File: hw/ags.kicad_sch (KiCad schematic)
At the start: 23 parts, among them J1 Screw_Terminal_01x08, J2 SWD/ARM10, J3 Conn_02x03_Odd_Even, J4 Conn_01x05, SW1 PTS526SM15SMTR2 LFS, U12 NV24C08DWVLT3G, U5 ESP32-S3-MINI-1

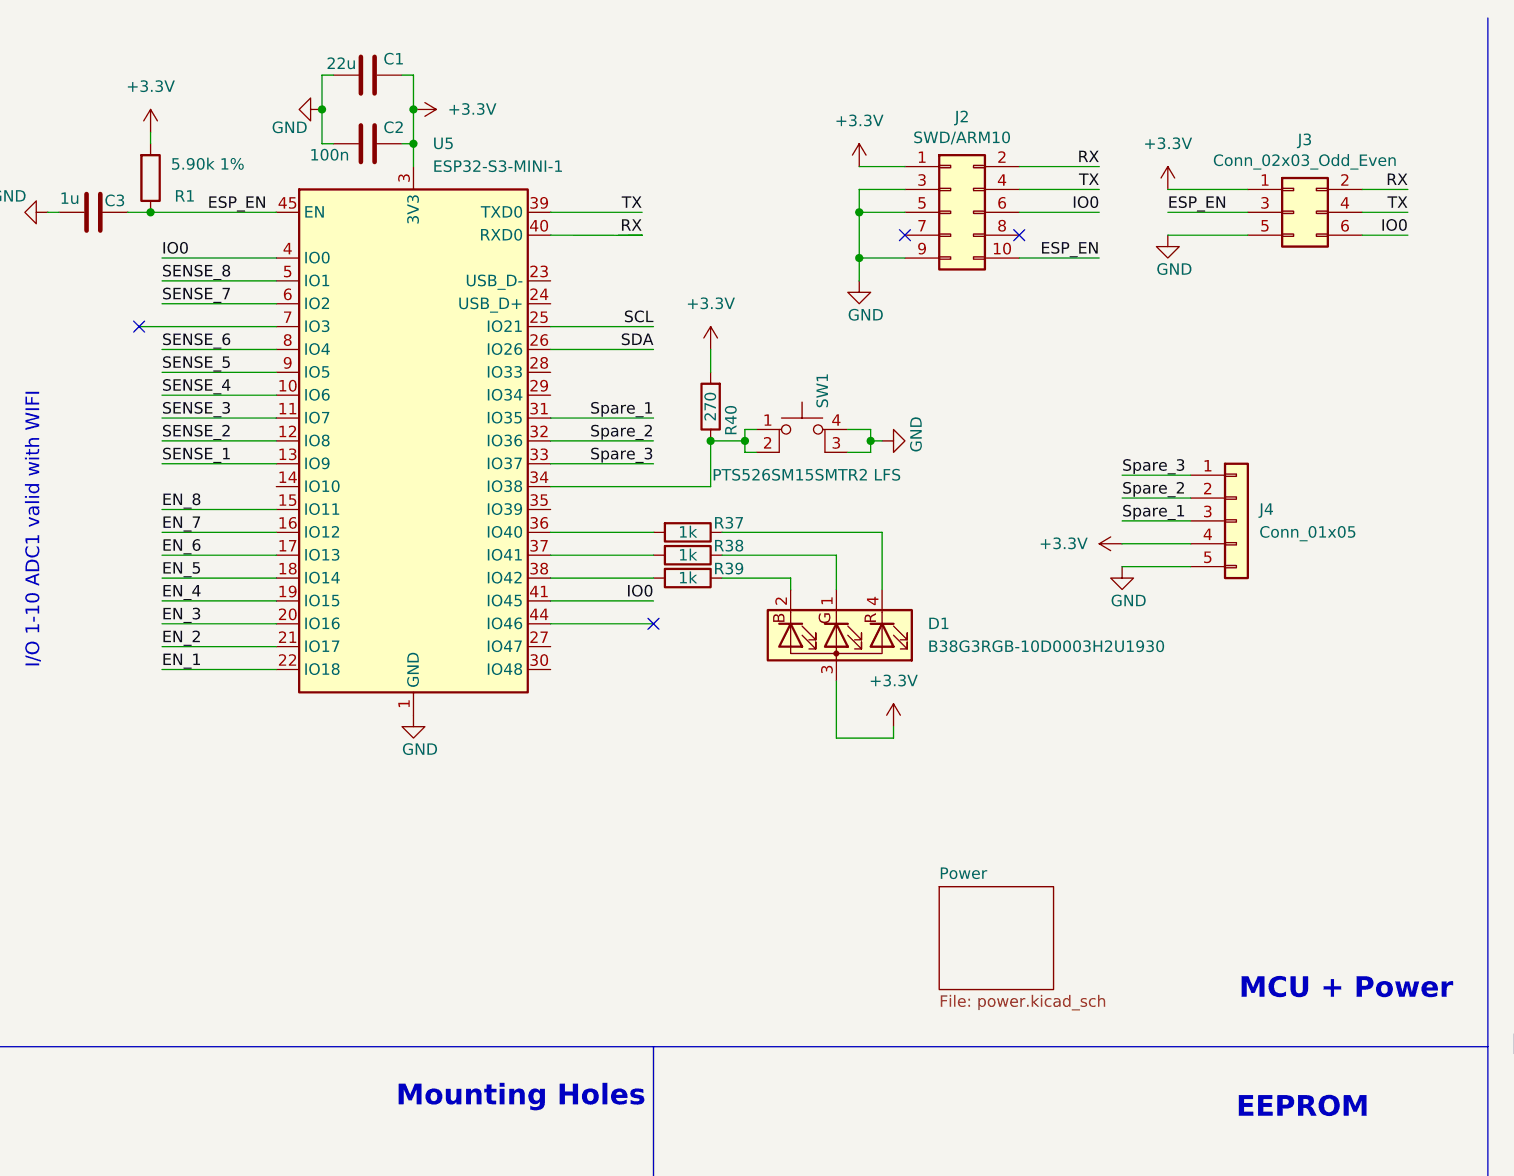
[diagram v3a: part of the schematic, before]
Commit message: Added sense for input voltage and created BOM
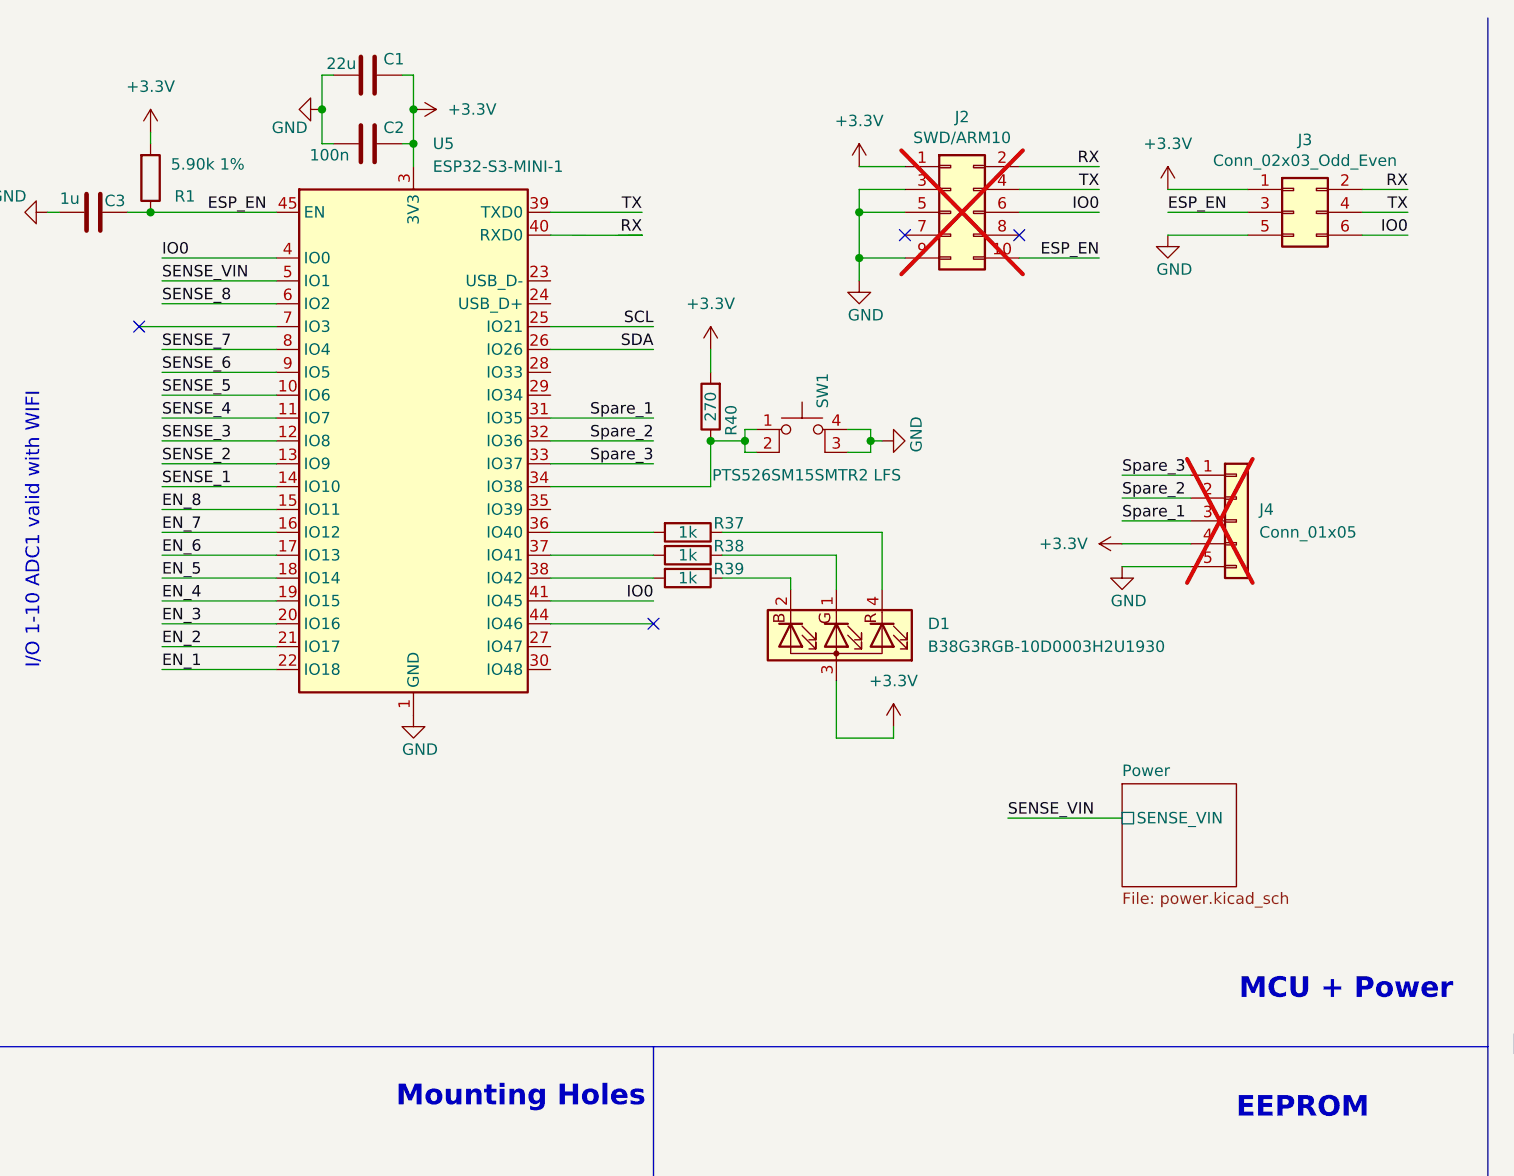
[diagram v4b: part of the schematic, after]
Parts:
- C1: Manufacturer Part Number (none) -> JMK212BBJ226MGHT
- C2: Manufacturer Part Number (none) -> CL10B104KC8NNNC
- C3, C4: Manufacturer Part Number (none) -> CL10B105KP8NNNC
- D1: Manufacturer Part Number (none) -> B38G3RGB-10D0003H2U1930
- J1: Manufacturer Part Number (none) -> QT08ASF83H0000G
- J2, J4: now not fitted
- R1, R15, R19: Manufacturer Part Number (none) -> AC0603FR-075K9L
- R37, R38, R39: Manufacturer Part Number (none) -> RMCF0603JT1K00
- R40: Manufacturer Part Number (none) -> RMCF0603JT270R
- SW1: Manufacturer Part Number (none) -> PTS526SM15SMTR2 LFS
- U12: Manufacturer Part Number (none) -> NV24C08DWVLT3G
- U5: Manufacturer Part Number (none) -> ESP32-S3-MINI-1-N8
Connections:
- net SENSE_1: now also U5.14 (IO10); no longer U5.13 (IO9)
- net SENSE_2: now also U5.13 (IO9); no longer U5.12 (IO8)
- net SENSE_3: now also U5.12 (IO8); no longer U5.11 (IO7)
- net SENSE_4: now also U5.11 (IO7); no longer U5.10 (IO6)
- net SENSE_5: now also U5.10 (IO6); no longer U5.9 (IO5)
- net SENSE_6: now also U5.9 (IO5); no longer U5.8 (IO4)
- net SENSE_7: now also U5.8 (IO4); no longer U5.6 (IO2)
- net SENSE_8: now also U5.6 (IO2); no longer U5.5 (IO1)
- new net SENSE_VIN: U5.5 (IO1)
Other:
- sheet Power ports: added SENSE_VIN; removed none
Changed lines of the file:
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@@
 	(wire
 		(pts
+			(xy 33.02 64.77) (xy 45.72 64.77)
+		)
+		(stroke
+			(width 0)
+			(type default)
+		)
+	)
+	(wire
+		(pts
 			(xy 115.57 29.21) (xy 110.49 29.21)
 		)
@@
 	(wire
 		(pts
+			(xy 127 101.6) (xy 139.7 101.6)
+		)
+		(stroke
+			(width 0)
+			(type default)
+		)
+	)
+	(wire
+		(pts
 			(xy 236.22 41.91) (xy 248.92 41.91)
 		)
@@
 	)
 	(label "SENSE_2"
-		(at 33.02 59.69 0)
+		(at 33.02 62.23 0)
 		(effects
 			(font
@@
 	)
 	(label "SENSE_1"
-		(at 33.02 62.23 0)
+		(at 33.02 64.77 0)
 		(effects
 			(font
@@
 	)
 	(label "SENSE_4"
-		(at 33.02 54.61 0)
+		(at 33.02 57.15 0)
 		(effects
 			(font
@@
 		)
 	)
+	(label "SENSE_VIN"
+		(at 127 101.6 0)
+		(effects
+			(font
+				(size 1.27 1.27)
+			)
+			(justify left bottom)
+		)
+	)
 	(label "COMM_V"
 		(at 238.76 74.93 0)
@@
 	)
 	(label "SENSE_8"
-		(at 33.02 41.91 0)
+		(at 33.02 44.45 0)
 		(effects
 			(font
@@
 		)
 	)
+	(label "SENSE_VIN"
+		(at 33.02 41.91 0)
+		(effects
+			(font
+				(size 1.27 1.27)
+			)
+			(justify left bottom)
+		)
+	)
 	(label "TX"
 		(at 171.45 34.29 180)
@@
 	)
 	(label "SENSE_6"
-		(at 33.02 49.53 0)
+		(at 33.02 52.07 0)
 		(effects
 			(font
@@
 	)
 	(label "SENSE_3"
-		(at 33.02 57.15 0)
+		(at 33.02 59.69 0)
 		(effects
 			(font
@@
 	)
 	(label "SENSE_7"
-		(at 33.02 44.45 0)
+		(at 33.02 49.53 0)
 		(effects
 			(font
@@
 	)
 	(label "SENSE_5"
-		(at 33.02 52.07 0)
+		(at 33.02 54.61 0)
 		(effects
 			(font
@@
 		(in_bom yes)
 		(on_board yes)
-		(dnp no)
+		(dnp yes)
 		(property "Reference" "J2"
 			(at 121.92 23.6982 0)
@@
 			)
 		)
+		(property "Manufacturer Part Number" "RMCF0603JT1K00"
+			(at 91.44 72.39 90)
+			(effects
+				(font
+					(size 1.27 1.27)
+				)
+				(hide yes)
+			)
+		)
 		(pin "1"
 		)
@@
 			)
 		)
+		(property "Manufacturer Part Number" "CL10B104KC8NNNC"
+			(at 55.88 26.67 90)
+			(effects
+				(font
+					(size 1.27 1.27)
+				)
+				(hide yes)
+			)
+		)
 		(pin "1"
 		)
@@
 			)
 		)
+		(property "Manufacturer Part Number" "B38G3RGB-10D0003H2U1930"
+			(at 107.95 81.28 90)
+			(effects
+				(font
+					(size 1.27 1.27)
+				)
+				(hide yes)
+			)
+		)
 		(pin "3"
 		)
@@
 			)
 		)
+		(property "Manufacturer Part Number" "AC0603FR-075K9L"
+			(at 162.56 158.75 0)
+			(effects
+				(font
+					(size 1.27 1.27)
+				)
+				(hide yes)
+			)
+		)
 		(pin "1"
 		)
@@
 			)
 		)
+		(property "Manufacturer Part Number" "AC0603FR-075K9L"
+			(at 31.75 30.48 0)
+			(effects
+				(font
+					(size 1.27 1.27)
+				)
+				(hide yes)
+			)
+		)
 		(pin "1"
 		)
@@
 			)
 		)
+		(property "Manufacturer Part Number" "RMCF0603JT1K00"
+			(at 91.44 69.85 90)
+			(effects
+				(font
+					(size 1.27 1.27)
+				)
+				(hide yes)
+			)
+		)
 		(pin "1"
 		)
@@
 			)
 		)
+		(property "Manufacturer Part Number" "JMK212BBJ226MGHT"
+			(at 55.88 19.05 90)
+			(effects
+				(font
+					(size 1.27 1.27)
+				)
+				(hide yes)
+			)
+		)
 		(pin "1"
 		)
@@
 			)
 		)
+		(property "Manufacturer Part Number" "CL10B105KP8NNNC"
+			(at 109.22 167.64 90)
+			(effects
+				(font
+					(size 1.27 1.27)
+				)
+				(hide yes)
+			)
+		)
 		(pin "1"
 		)
@@
 			)
 		)
+		(property "Manufacturer Part Number" "NV24C08DWVLT3G"
+			(at 123.19 168.91 0)
+			(effects
+				(font
+					(size 1.27 1.27)
+				)
+				(hide yes)
+			)
+		)
 		(pin "3"
 		)
@@
 			)
 		)
+		(property "Manufacturer Part Number" "AC0603FR-075K9L"
+			(at 148.59 158.75 0)
+			(effects
+				(font
+					(size 1.27 1.27)
+				)
+				(hide yes)
+			)
+		)
 		(pin "1"
 		)
@@
 			)
 		)
+		(property "Manufacturer Part Number" "RMCF0603JT270R"
+			(at 93.98 55.88 90)
+			(effects
+				(font
+					(size 1.27 1.27)
+				)
+				(hide yes)
+			)
+		)
 		(pin "1"
 		)
@@
 		(in_bom yes)
 		(on_board yes)
-		(dnp no)
+		(dnp yes)
 		(fields_autoplaced yes)
 		(property "Reference" "J4"
@@
 			)
 		)
+		(property "Manufacturer Part Number" "ESP32-S3-MINI-1-N8"
+			(at 60.96 59.69 0)
+			(effects
+				(font
+					(size 1.27 1.27)
+				)
+				(hide yes)
+			)
+		)
 		(pin "7"
 		)
@@
 			)
 		)
+		(property "Manufacturer Part Number" "CL10B105KP8NNNC"
+			(at 25.4 34.29 90)
+			(effects
+				(font
+					(size 1.27 1.27)
+				)
+				(hide yes)
+			)
+		)
 		(pin "1"
 		)
@@
 			)
 		)
+		(property "Manufacturer Part Number" "QT08ASF83H0000G"
+			(at 219.71 137.16 0)
+			(effects
+				(font
+					(size 1.27 1.27)
+				)
+				(hide yes)
+			)
+		)
 		(pin "6"
 		)
@@
 			)
 		)
+		(property "Manufacturer Part Number" "PTS526SM15SMTR2 LFS"
+			(at 104.14 60.96 90)
+			(effects
+				(font
+					(size 1.27 1.27)
+				)
+				(hide yes)
+			)
+		)
 		(pin "3"
 		)
@@
 			)
 		)
+		(property "Manufacturer Part Number" "RMCF0603JT1K00"
+			(at 91.44 74.93 90)
+			(effects
+				(font
+					(size 1.27 1.27)
+				)
+				(hide yes)
+			)
+		)
 		(pin "1"
 		)
@@
 	)
 	(sheet
-		(at 119.38 109.22)
+		(at 139.7 97.79)
 		(size 12.7 11.43)
 		(exclude_from_sim no)
@@
 		)
 		(property "Sheetname" "Power"
-			(at 119.38 108.5084 0)
+			(at 139.7 97.0784 0)
 			(effects
 				(font
@@
 		)
 		(property "Sheetfile" "power.kicad_sch"
-			(at 119.38 121.2346 0)
+			(at 139.7 109.8046 0)
 			(effects
 				(font
@@
 			)
 		)
+		(pin "SENSE_VIN" passive
+			(at 139.7 101.6 180)
+			(effects
+				(font
+					(size 1.27 1.27)
+				)
+				(justify left)
+			)
+		)

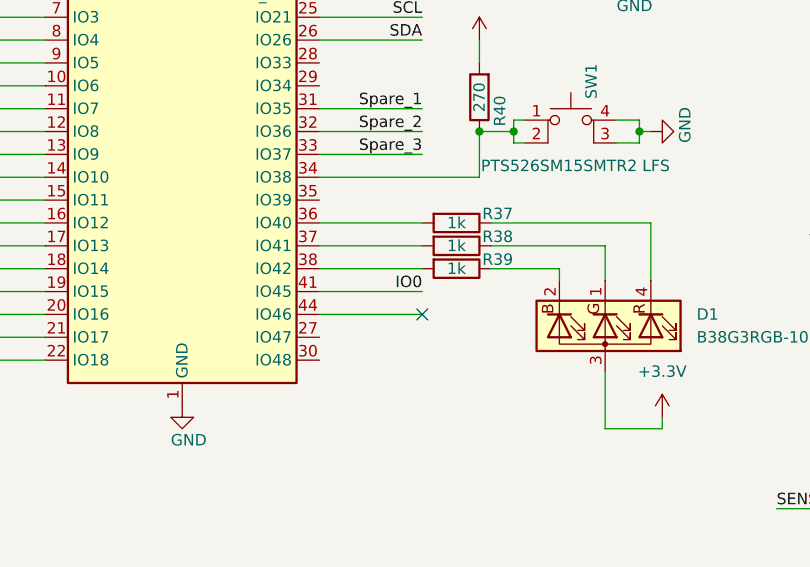
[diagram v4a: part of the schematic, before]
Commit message: Fixed button footprint and layout, fixed IO0 layout, widened connector holes
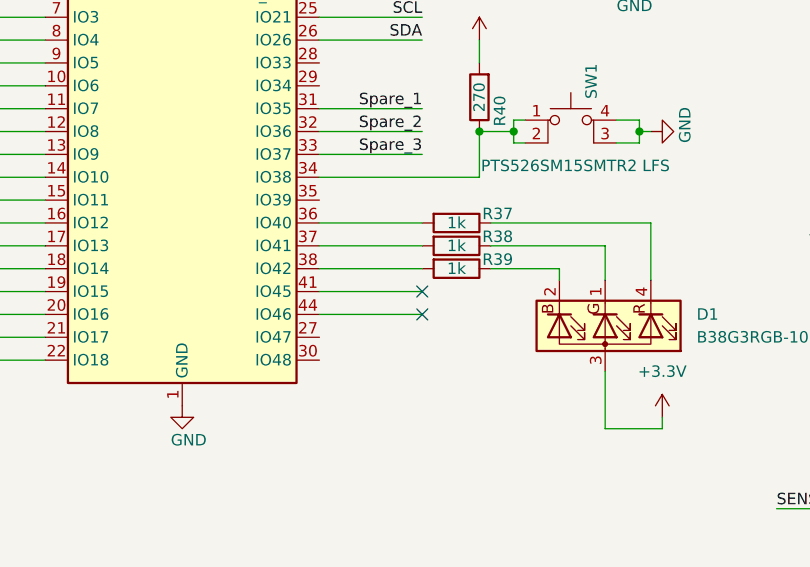
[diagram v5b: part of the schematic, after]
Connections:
- net IO0: no longer U5.41 (IO45)
- no-connect marks 4 -> 5
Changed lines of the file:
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@@
+	)
+	(no_connect
+		(at 87.63 77.47)
 	)
 	(no_connect
@@
 		)
 	)
-	(label "IO0"
-		(at 87.63 77.47 180)
-		(effects
-			(font
-				(size 1.27 1.27)
-			)
-			(justify right bottom)
-		)
-	)
